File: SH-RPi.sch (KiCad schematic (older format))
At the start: 0 parts

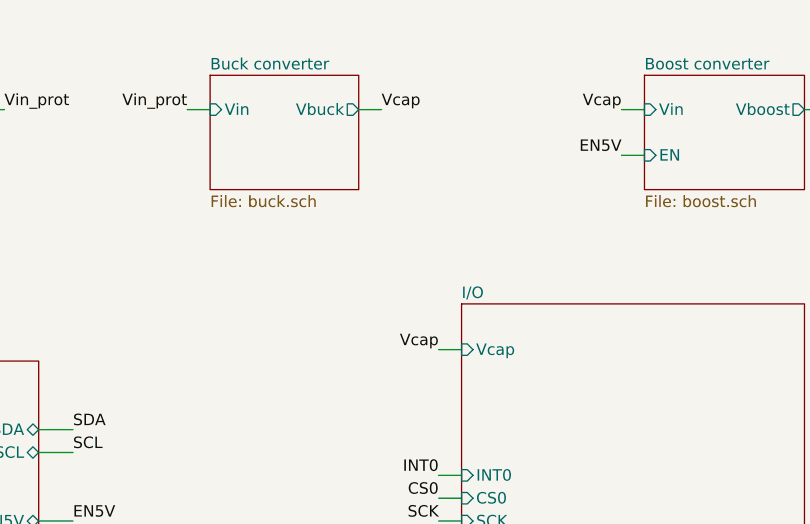
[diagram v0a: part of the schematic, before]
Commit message: Extend the PCB size to provide space for an onboard supercapacitor
The PCB was extended to the left by 21mm to provide room for a
18x40mm (max 18x42mm) 50/60F supercapacitor. The supercapacitor
is lodged in a slot on the PCB to provide mechanical stability and limit
the maximum height of the assembly. It now requires 14mm of headroom.

Additionally, the following changes were made:

- the external supercap connector was removed
- the power and CAN connectors were swapped to JST XH
- there is space for a wire link between CAN and power conx
- power protection circuitry was moved to the edge of the board
- 3.3V regulator was moved to improve the layout
- a 100pF cap was added to the boost feedback to improve loop stability
- rectangles were drawn around ground pins on the GPIO connector
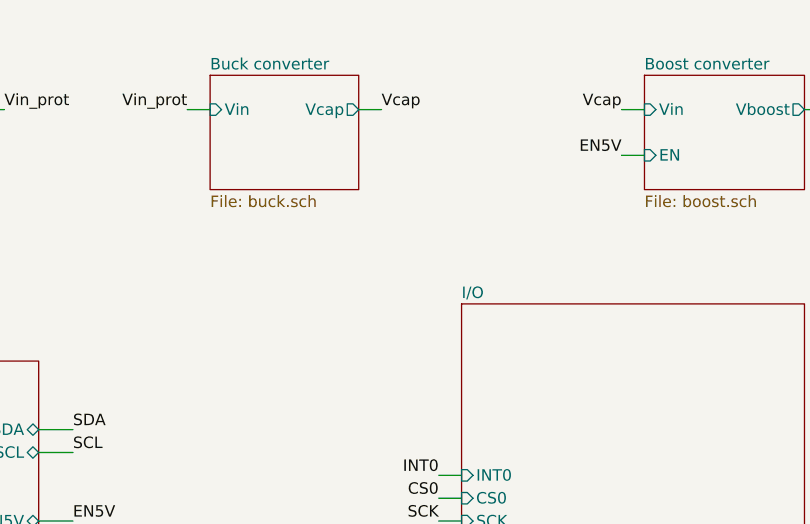
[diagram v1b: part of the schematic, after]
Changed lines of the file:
@@
 Title "Sailor Hat for Raspberry Pi"
 Date ""
-Rev "revL"
+Rev "revM"
 Comp "Hat Laboratories"
 Comment1 "https://creativecommons.org/licenses/by-sa/4.0"
@@
 F1 "buck.sch" 50
 F2 "Vin" I L 3200 1300 50
-F3 "Vbuck" O R 3850 1300 50
+F3 "Vcap" O R 3850 1300 50
 $EndSheet
 Text Label 5000 1500 2    50   ~ 0
@@
 F4 "ATT_LED1" I L 4300 4750 50
 F5 "ATT_LED0" I L 4300 4650 50
-F6 "Vcap" I L 4300 2350 50
-F7 "INT0" I L 4300 2900 50
-F8 "CS0" I L 4300 3000 50
-F9 "SCK" I L 4300 3100 50
-F10 "SO" I L 4300 3300 50
-F11 "SI" I L 4300 3200 50
-F12 "SDA" I L 4300 3650 50
-F13 "SCL" I L 4300 3750 50
+F6 "INT0" I L 4300 2900 50
+F7 "CS0" I L 4300 3000 50
+F8 "SCK" I L 4300 3100 50
+F9 "SO" I L 4300 3300 50
+F10 "SI" I L 4300 3200 50
+F11 "SDA" I L 4300 3650 50
+F12 "SCL" I L 4300 3750 50
 $EndSheet
 $Sheet
@@
 Text Label 1250 2500 2    50   ~ 0
 Vin_prot
-Text Label 4200 2350 2    50   ~ 0
-Vcap
 Text Label 4200 2900 2    50   ~ 0
 INT0
@@
 Wire Wire Line
 	4200 5050 4300 5050
-Wire Wire Line
-	4200 2350 4300 2350
 $Sheet
 S 4300 5800 1500 450

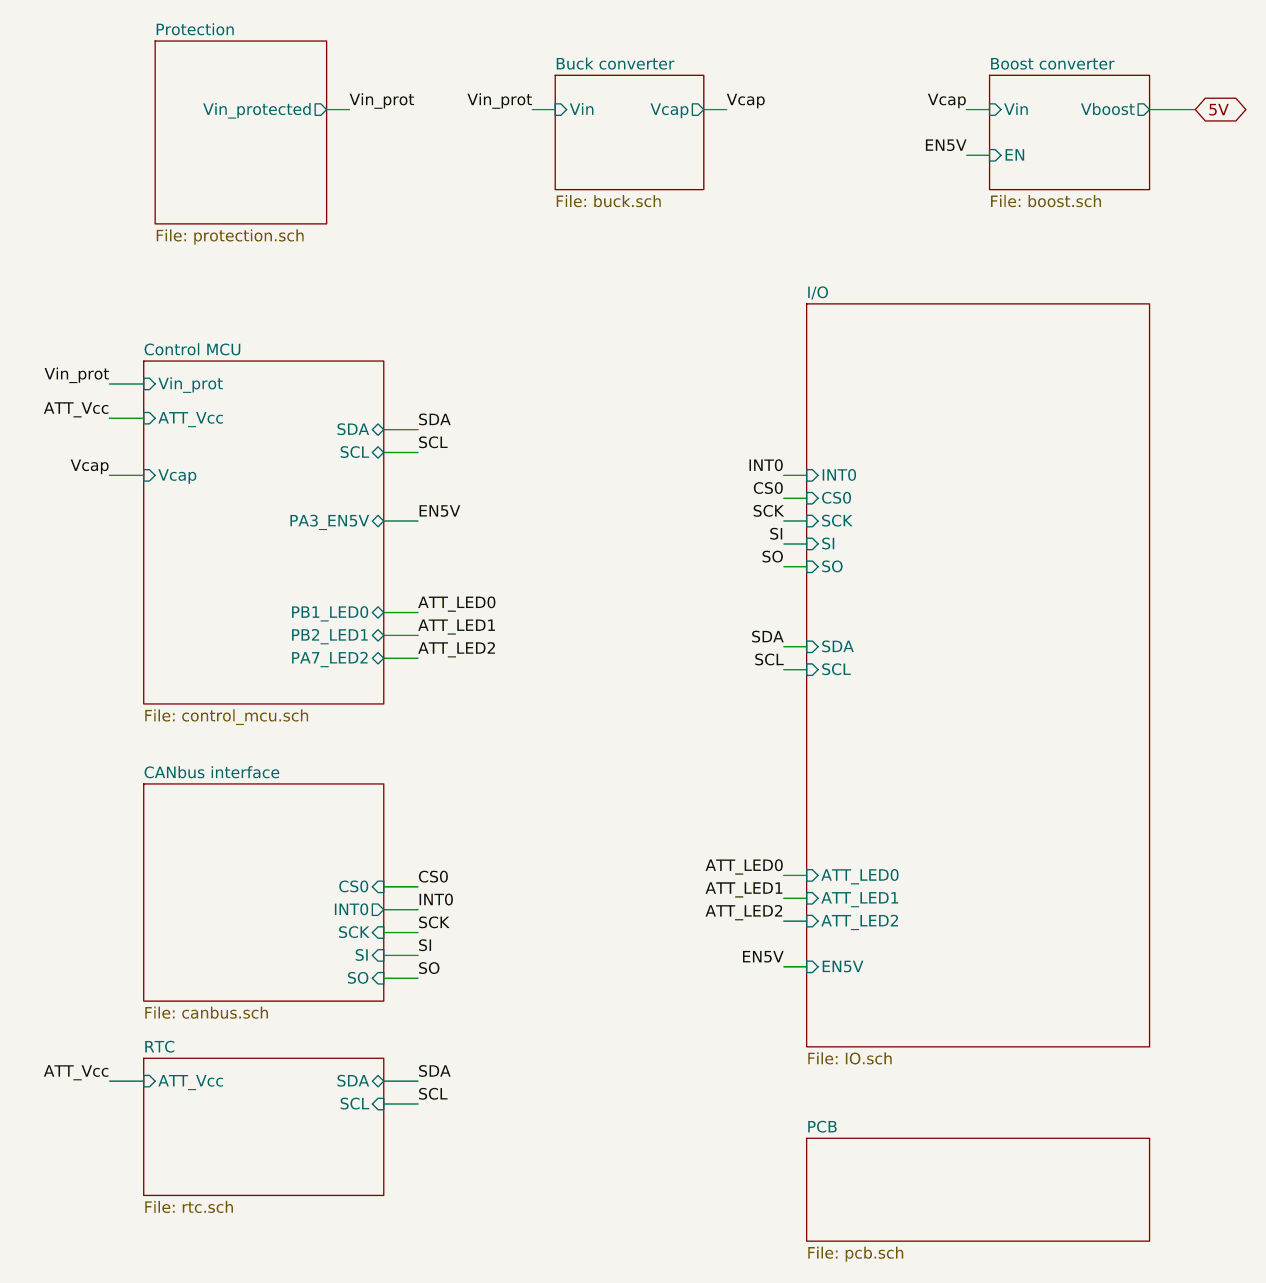
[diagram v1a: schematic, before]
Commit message: Route I2C to unique pins
Also:
- Connect RTC interrupt to ATtiny
- Break out the interrupt pin to a connector for external signaling
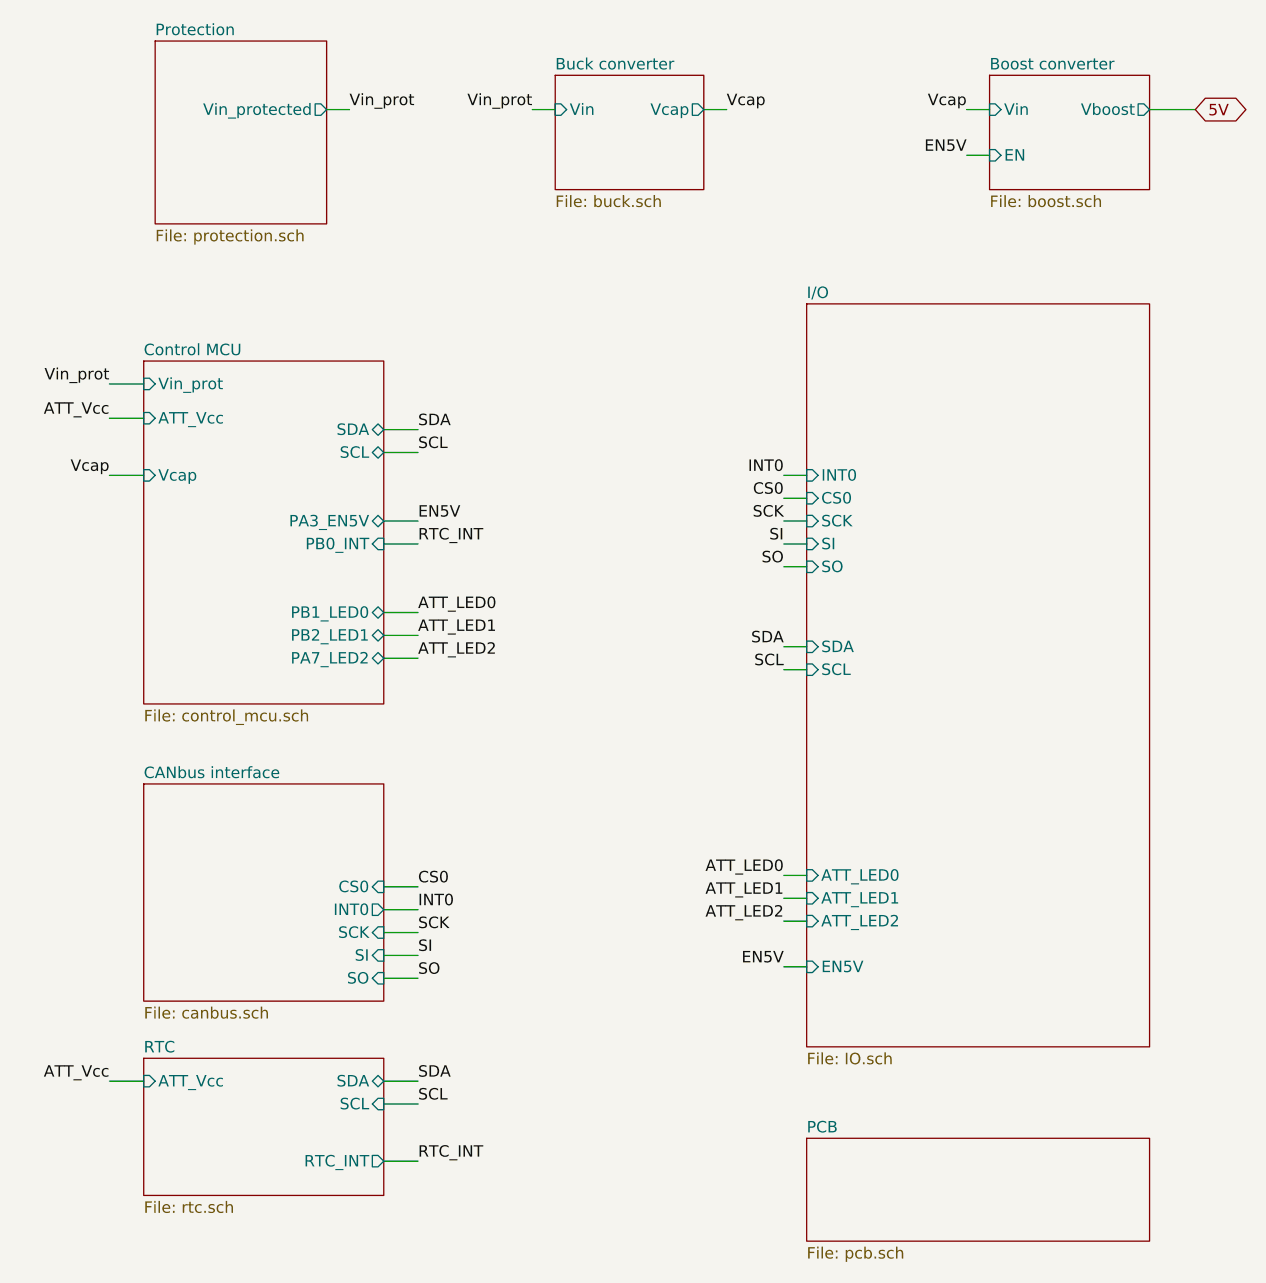
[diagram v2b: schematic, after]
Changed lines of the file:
@@
 F3 "SDA" B R 2450 5550 50
 F4 "ATT_Vcc" I L 1400 5550 50
+F5 "RTC_INT" O R 2450 5900 50
 $EndSheet
 Wire Wire Line
@@
 F9 "ATT_Vcc" I L 1400 2650 50
 F10 "Vcap" I L 1400 2900 50
+F11 "PB0_INT" I R 2450 3200 50
 $EndSheet
 Wire Wire Line
@@
 Wire Wire Line
 	1250 5550 1400 5550
+Wire Wire Line
+	2450 5900 2600 5900
+Text Label 2600 5900 0    50   ~ 0
+RTC_INT
+Wire Wire Line
+	2450 3200 2600 3200
+Text Label 2600 3200 0    50   ~ 0
+RTC_INT
 $EndSCHEMATC

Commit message: Change the MCU to ATTiny1614
Also:
- Rewired the PCB due to changed pins
- Cleaned up network names around the MCU
- Use a basic part Schottky for the buck converter
- Change MCP2515 crystal to 16MHz basic part
- Change BAT54C to two discrete schottkys
- Change the SOD-523 schottky to MSK4005
- Update the release script and rotation DB
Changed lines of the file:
@@
 EN5V
 Text Label 2600 3700 0    50   ~ 0
-ATT_LED2
+ATT_LED_VIN
 Text Label 2600 2800 0    50   ~ 0
 SCL
@@
 SDA
 Text Label 2600 3600 0    50   ~ 0
-ATT_LED1
+ATT_LED_VCAP
 Wire Wire Line
 	2600 2700 2450 2700
@@
 	1250 2650 1400 2650
 Text Label 2600 3500 0    50   ~ 0
-ATT_LED0
+ATT_LED_STATUS
 Text GLabel 6000 1300 2    50   BiDi ~ 0
 5V
@@
 F3 "SDA" B R 2450 2700 50
 F4 "SCL" B R 2450 2800 50
-F5 "PA7_LED2" B R 2450 3700 50
-F6 "PA3_EN5V" B R 2450 3100 50
-F7 "PB1_LED0" B R 2450 3500 50
-F8 "PB2_LED1" B R 2450 3600 50
+F5 "LED_VIN" B R 2450 3700 50
+F6 "EN5V" B R 2450 3100 50
+F7 "LED_STATUS" B R 2450 3500 50
+F8 "LED_VCAP" B R 2450 3600 50
 F9 "ATT_Vcc" I L 1400 2650 50
 F10 "Vcap" I L 1400 2900 50
-F11 "PB0_INT" I R 2450 3200 50
+F11 "EXT_INT" I R 2450 3200 50
 $EndSheet
 Wire Wire Line
@@
 F0 "I/O" 50
 F1 "IO.sch" 50
-F2 "ATT_LED2" I L 4300 4850 50
+F2 "ATT_LED_VIN" I L 4300 4850 50
 F3 "EN5V" I L 4300 5050 50
-F4 "ATT_LED1" I L 4300 4750 50
-F5 "ATT_LED0" I L 4300 4650 50
+F4 "ATT_LED_VCAP" I L 4300 4750 50
+F5 "ATT_LED_STATUS" I L 4300 4650 50
 F6 "INT0" I L 4300 2900 50
 F7 "CS0" I L 4300 3000 50
@@
 	4200 3300 4300 3300
 Text Label 4200 4850 2    50   ~ 0
-ATT_LED2
+ATT_LED_VIN
 Text Label 4200 4750 2    50   ~ 0
-ATT_LED1
+ATT_LED_VCAP
 Wire Wire Line
 	4300 4850 4200 4850
@@
 	4300 4750 4200 4750
 Text Label 4200 4650 2    50   ~ 0
-ATT_LED0
+ATT_LED_STATUS
 Text Label 4200 5050 2    50   ~ 0
 EN5V
